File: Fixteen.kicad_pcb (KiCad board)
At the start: 2 copper layers, 25.4 x 62.7 mm, 9 parts, among them J1 TED_SOCKET, J2 CAS_EXT_CONN, J98 KICAD_LOGO, J99 OSHW_LOGO, U1 MOS_7360_TED, U2 74LS253

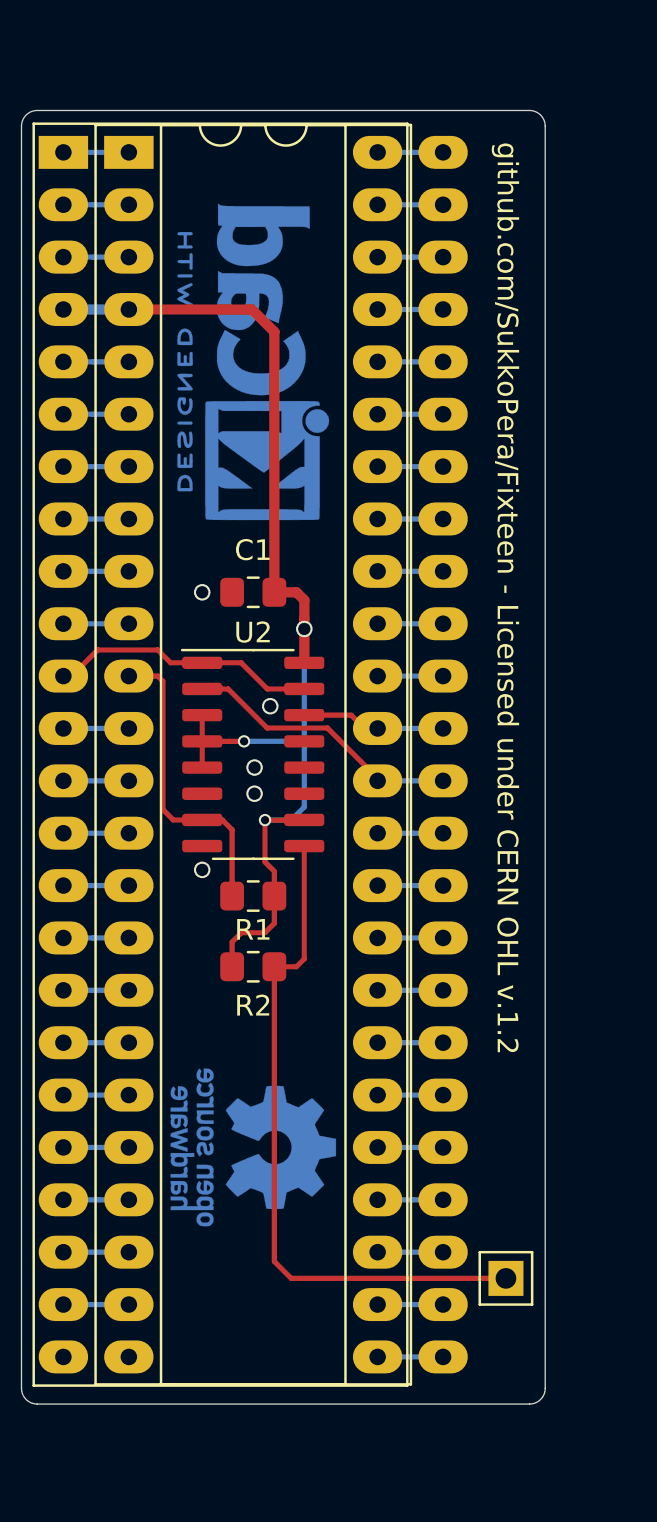
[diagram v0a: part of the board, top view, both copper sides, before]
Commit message: Add ESD protection (?) Found all of this stuff uncommitted after months... :|
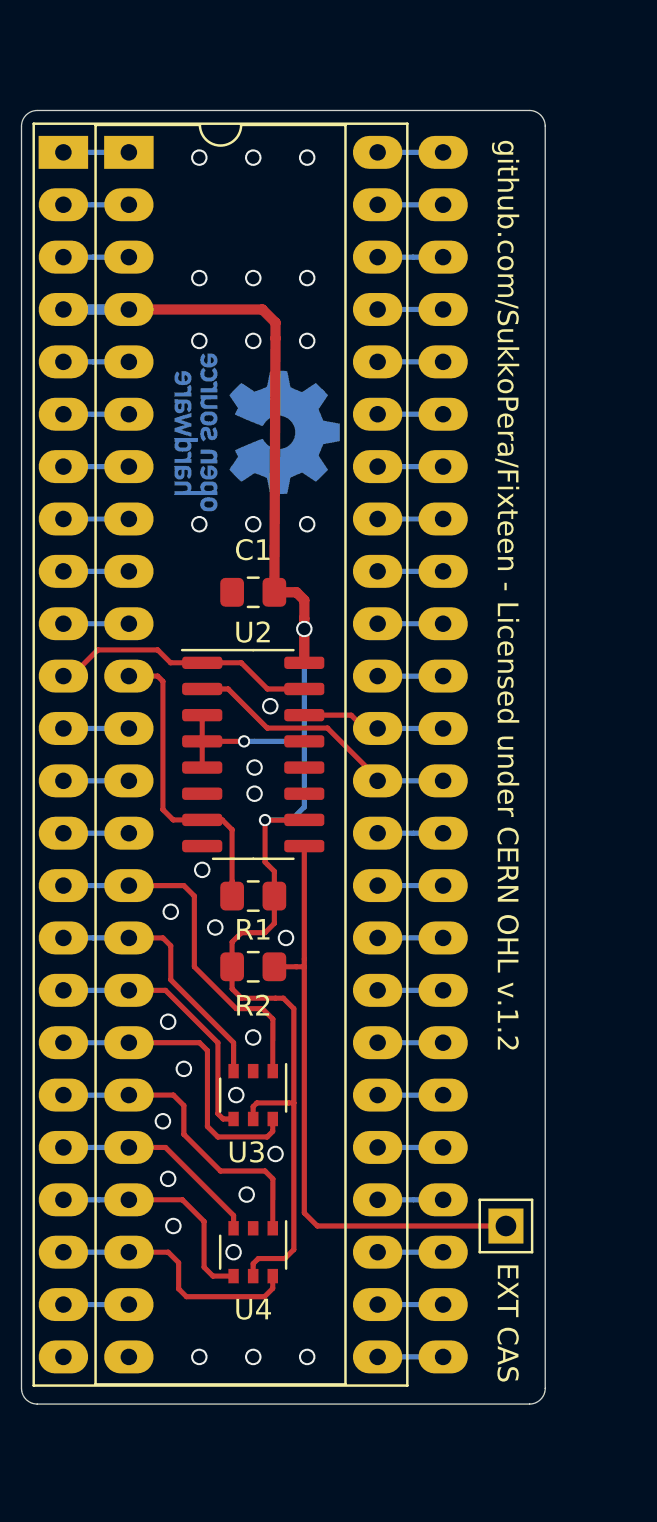
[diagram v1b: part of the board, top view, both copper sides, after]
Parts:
- removed J98: KICAD_LOGO, Symbol:KiCad-Logo2_6mm_Copper
- added U3: DT1042, Package_SO:TSOP-6_1.65x3.05mm_P0.95mm, F.Cu at (131.1, 121.7)
- added U4: DT1042, Package_SO:TSOP-6_1.65x3.05mm_P0.95mm, F.Cu at (131.1, 129.3)
- J1: footprint Package_DIP:DIP-48_W15.24mm_LongPads -> Fixteen:DIP-48_W15.24mm_LongPads_ModSilkS
- moved J99 34.7 mm to (131.3, 89.5)
- moved J2 2.54 mm to (143.4, 128.0)
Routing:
- net VCC: track 57.1 -> 79.0 mm
- net /k0: track 3.17 -> 17.4 mm
- net /k4: track 3.17 -> 15.1 mm
- net /k3: track 3.17 -> 14.9 mm
- net /k2: track 3.17 -> 12.9 mm
- net /k1: track 3.17 -> 12.7 mm
- net /k7: track 3.17 -> 12.6 mm
- net /k6: track 3.17 -> 11.1 mm
- net /k5: track 3.17 -> 10.2 mm
- net /~cas_ext: track 33.9 -> 29.3 mm
- net GND: vias 5 -> 32
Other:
- board text added: "EXT CAS"
- board text added: "V1"

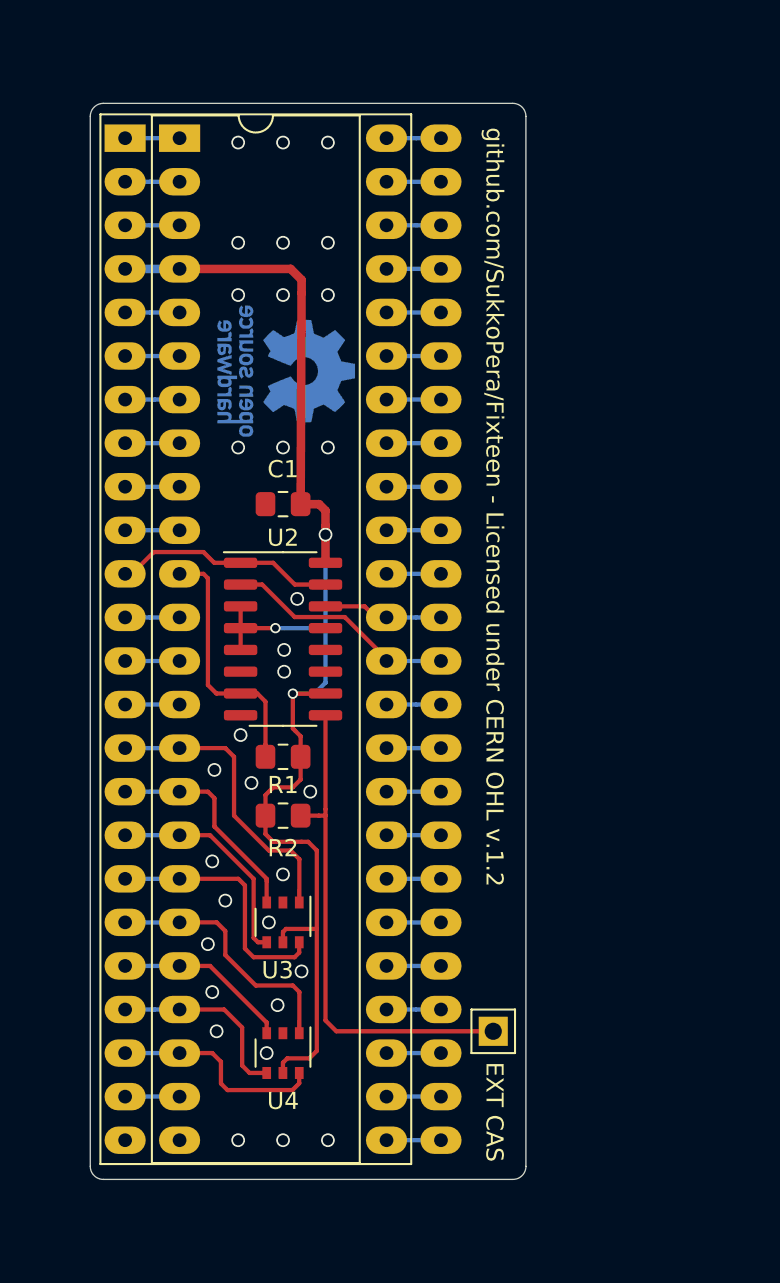
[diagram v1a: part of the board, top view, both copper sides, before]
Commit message: Turned this into a ESD protection + 64k internal RAM expansion
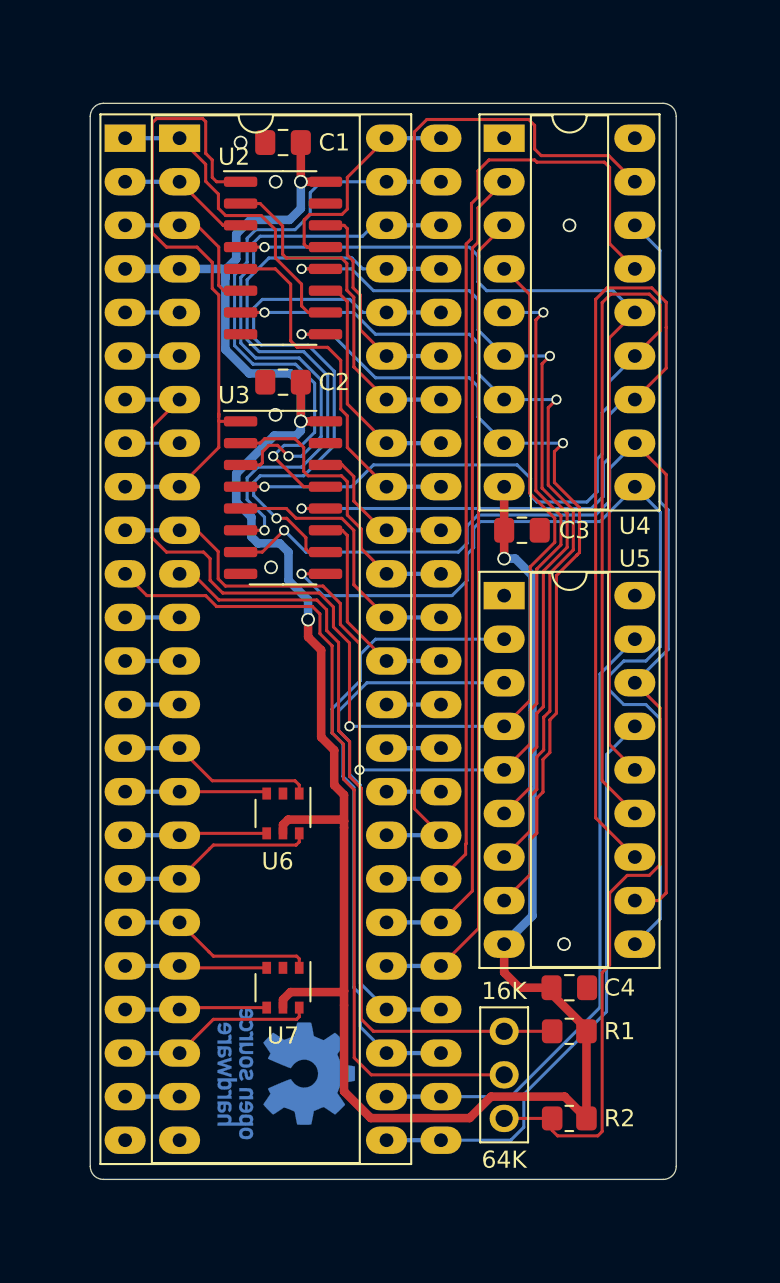
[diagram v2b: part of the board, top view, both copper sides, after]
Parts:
- added C2: 100n, Capacitor_SMD:C_0805_2012Metric_Pad1.18x1.45mm_HandSolder, F.Cu at (131.1, 90.2)
- added C3: 100n, Capacitor_SMD:C_0805_2012Metric_Pad1.18x1.45mm_HandSolder, F.Cu at (145.1, 98.8)
- added C4: 100n, Capacitor_SMD:C_0805_2012Metric_Pad1.18x1.45mm_HandSolder, F.Cu at (147.8, 125.5)
- added U3: 74LS257, Package_SO:SOIC-16_3.9x9.9mm_P1.27mm, F.Cu at (131.1, 96.9)
- added U4: 4464, Package_DIP:DIP-18_W7.62mm_Socket_LongPads, F.Cu at (144.0, 75.9)
- added U5: 4464, Package_DIP:DIP-18_W7.62mm_Socket_LongPads, F.Cu at (144.0, 102.6)
- C1: footprint Capacitor_SMD:C_0805_2012Metric_Pad1.15x1.40mm_HandSolder -> Capacitor_SMD:C_0805_2012Metric_Pad1.18x1.45mm_HandSolder
- J2: value CAS_EXT_CONN -> RAM_SELECTOR; footprint Fixteen:PinHeader_1x01_P2.54mm_Vertical -> Fixteen:Pin_Header_Straight_1x03-ModSilkS
- R1, R2: footprint Resistor_SMD:R_0805_2012Metric_Pad1.15x1.40mm_HandSolder -> Resistor_SMD:R_0805_2012Metric_Pad1.20x1.40mm_HandSolder
- U2: value 74LS253 -> 74LS257
- moved J99 41.0 mm to (131.3, 130.5)
- moved R2 24.3 mm to (147.8, 133.1), turned to 180 degrees
- moved R1 23.1 mm to (147.8, 128.0)
- moved U2 22.2 mm to (131.1, 82.9)
- moved C1 21.1 mm to (131.1, 76.2)
- moved U6 6.35 mm to (131.1, 115.3)
- moved U7 3.81 mm to (131.1, 125.5)
- moved J2 0.63 mm to (144.0, 128.0)
- renumbered U3 to U6, U4 to U7
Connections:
- net /a12 renamed a12
- net /a13 renamed a13
- net /a4 renamed a4
- net /a5 renamed a5
- net /a6 renamed a6
- net /a7 renamed a7
- net /db0 renamed d0
- net /db1 renamed d1
- net /db2 renamed d2
- net /db3 renamed d3
- net /db4 renamed d4
- net /db5 renamed d5
- net /db6 renamed d6
- net /db7 renamed d7
- net /r~w renamed R_~W
- net /~ras renamed ~RAS
- J1 pad 1: /a2 -> a2
- J1 pad 11: /~cas_int -> /~cas_16k
- J1 pad 2: /a1 -> a1
- J1 pad 3: /a0 -> a0
- J1 pad 36: /a15 -> a15
- J1 pad 37: /a14 -> a14
- J1 pad 40: /a11 -> a11
- J1 pad 41: /a10 -> a10
- J1 pad 42: /a9 -> a9
- J1 pad 43: /a8 -> a8
- J1 pad 48: /a3 -> a3
- J1 pad 9: /mux -> SEL
- J2 pad 1: /~cas_ext -> /~cas_16k
- R1 pad 2: /~cas_int -> /~cas_16k
- R2 pad 2: /~cas_ext -> ~CAS_64K
- U1 pad 1: /a2 -> a2
- U1 pad 2: /a1 -> a1
- U1 pad 3: /a0 -> a0
- U1 pad 36: /a15 -> a15
- U1 pad 37: /a14 -> a14
- U1 pad 40: /a11 -> a11
- U1 pad 41: /a10 -> a10
- U1 pad 42: /a9 -> a9
- U1 pad 43: /a8 -> a8
- U1 pad 48: /a3 -> a3
- U1 pad 9: /mux -> SEL
- U2 pad 1: /~cas -> SEL
- U2 pad 10: VCC -> a2
- U2 pad 11: GND -> a10
- U2 pad 12: GND -> /64K RAM Expansion/m6
- U2 pad 13: GND -> a3
- U2 pad 14: /a14 -> a8
- U2 pad 15: /~cas -> GND
- U2 pad 2: /a15 -> a9
- U2 pad 3: VCC -> a1
- U2 pad 4: VCC -> /64K RAM Expansion/m0
- U2 pad 5: VCC -> a11
- U2 pad 6: GND -> a0
- U2 pad 7: /~cas_int -> /64K RAM Expansion/m5
- U2 pad 9: /~cas_ext -> /64K RAM Expansion/m4
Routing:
- net /64K RAM Expansion/m2: track 0.00 -> 70.7 mm, vias 0 -> 1
- net /64K RAM Expansion/m1: track 0.00 -> 69.9 mm, vias 0 -> 1
- net R_~W: track 3.17 -> 70.4 mm, vias 0 -> 1
- net VCC: track 79.0 -> 144.6 mm, vias 3 -> 4
- net ~CAS_64K: track 0.00 -> 63.9 mm
- net ~RAS: track 3.17 -> 65.0 mm, vias 0 -> 2
- net d7: track 3.18 -> 60.9 mm
- net /64K RAM Expansion/m7: track 0.00 -> 57.5 mm, vias 0 -> 1
- net /64K RAM Expansion/m3: track 0.00 -> 57.4 mm, vias 0 -> 1
- net d6: track 3.18 -> 60.0 mm
- net /64K RAM Expansion/m0: track 0.00 -> 53.3 mm, vias 0 -> 1
- net /64K RAM Expansion/m5: track 0.00 -> 50.7 mm, vias 0 -> 2
- net /64K RAM Expansion/m4: track 0.00 -> 49.6 mm, vias 0 -> 2
- net /64K RAM Expansion/m6: track 0.00 -> 48.0 mm, vias 0 -> 2
- net /~cas_16k: track 0.00 -> 45.6 mm
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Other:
- board size 25.4 x 62.7 mm -> 34.2 x 62.7 mm
- net class Default: clearance 0.2 -> 0.18; trace_width 0.25 -> 0.18
- rule trace_clearance: 0.2 -> 0.18
- rule trace_min: 0.2 -> 0.1524
- board text added: "16K"
- board text added: "64K"
- board text added: "V2"
- board text added: "github.com/SukkoPera/Fixteen Licensed under CERN OHL v.1.2"
- board text removed: "EXT CAS"
- board text removed: "V1"
- board text removed: "github.com/SukkoPera/Fixteen - Licensed under CERN OHL v.1.2"
